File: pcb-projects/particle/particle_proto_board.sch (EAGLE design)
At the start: 53 parts, among them IC1 ATTINY20-MMH, IC2 DMC2400V, IC3 DMC2400V, SW1 SW1, SW2 SW2, SW3 SW3

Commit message: added several sparkfun and one samtec library, fixed #39, fixed #37, fixed #36, fixed #35, fixed #29
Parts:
- removed PI: 332-06, con-garry:332-06
- removed R3, R7, R8: J5MM, jumper:J5MM
- added J1: FTS-103-01-L-DV, samtec-FTS-103-01-L-DV:FTS-103-01-L-DV
- RESET: value RESET -> SWITCH-MOMENTARY-2SMD; device jumper-switches:SJ -> SparkFun-Electromechanical:SWITCH-MOMENTARY-2SMD
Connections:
- removed net N$16: R8.1, SW3.2
- removed net N$19: PI-4.S, R8.2
- removed net N$21: PI-1.S, R3.2
- net GND: now also J1.6, RESET.1, SGNL_LED.C; no longer PI-6.S, RESET.2, SWLED1.1
- net N$1: now also J1.1; no longer R3.1
- net N$11: now also SWLED1.2; no longer R5.1
- net N$15: now also J1.4, SW3.2; no longer PI-3.S, R7.2
- net N$20: now also J1.3; no longer R7.1
- net N$23: now also R5.1, SWLED1.1; no longer SGNL_LED.C, SWLED1.2
- net RESET: now also J1.5, RESET.2; no longer PI-5.S, RESET.1
- net VCC: now also J1.2; no longer PI-2.S
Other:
- moved on the sheet: C1, GND_A, GND_B, IC1B, IC2A, IC2B, IC3A, IC3B, PWR/TX_A, PWR/TX_B, PWR_LED, R1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

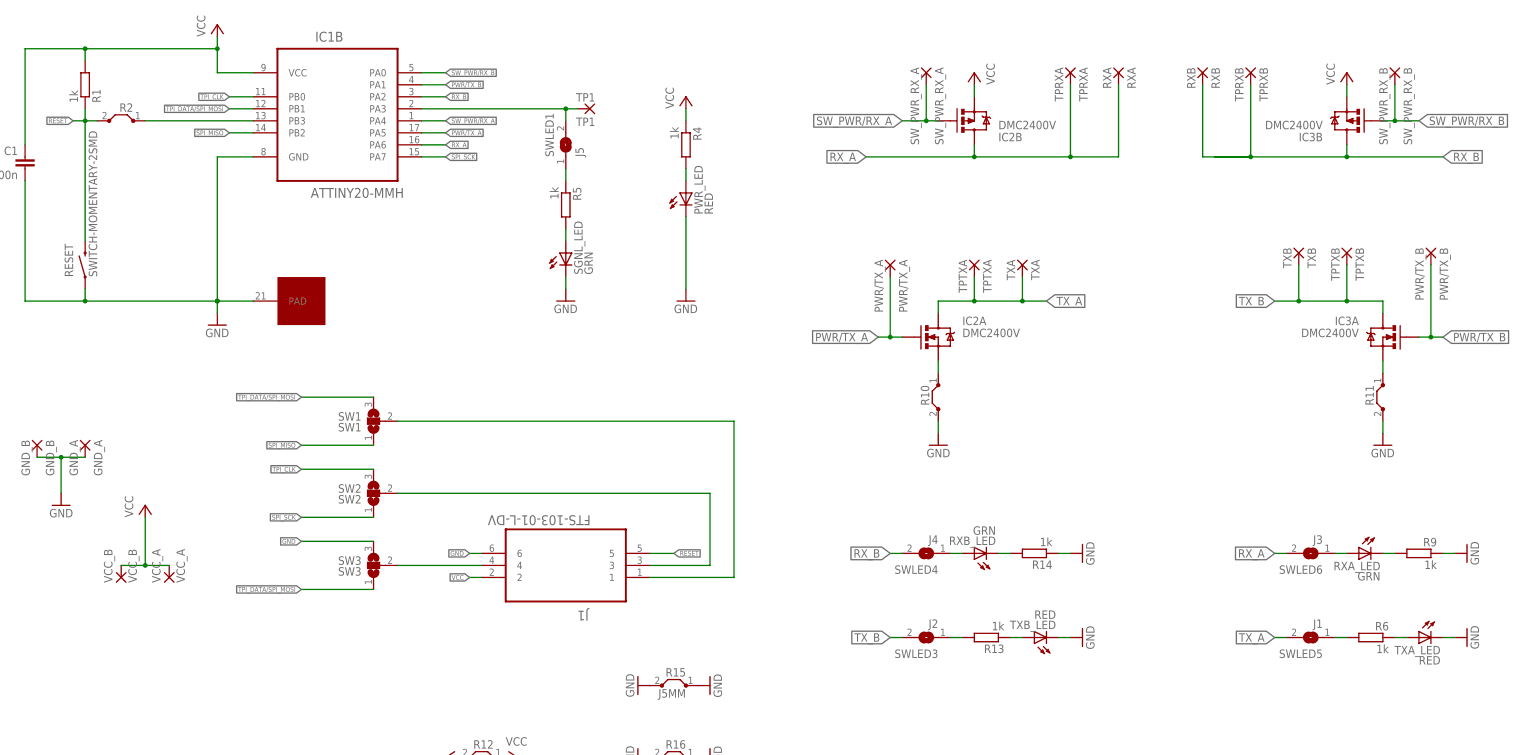
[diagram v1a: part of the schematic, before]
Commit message: fixed #41, fixed #40, fixed #39, fixed #37, fixed #35, fixed #29
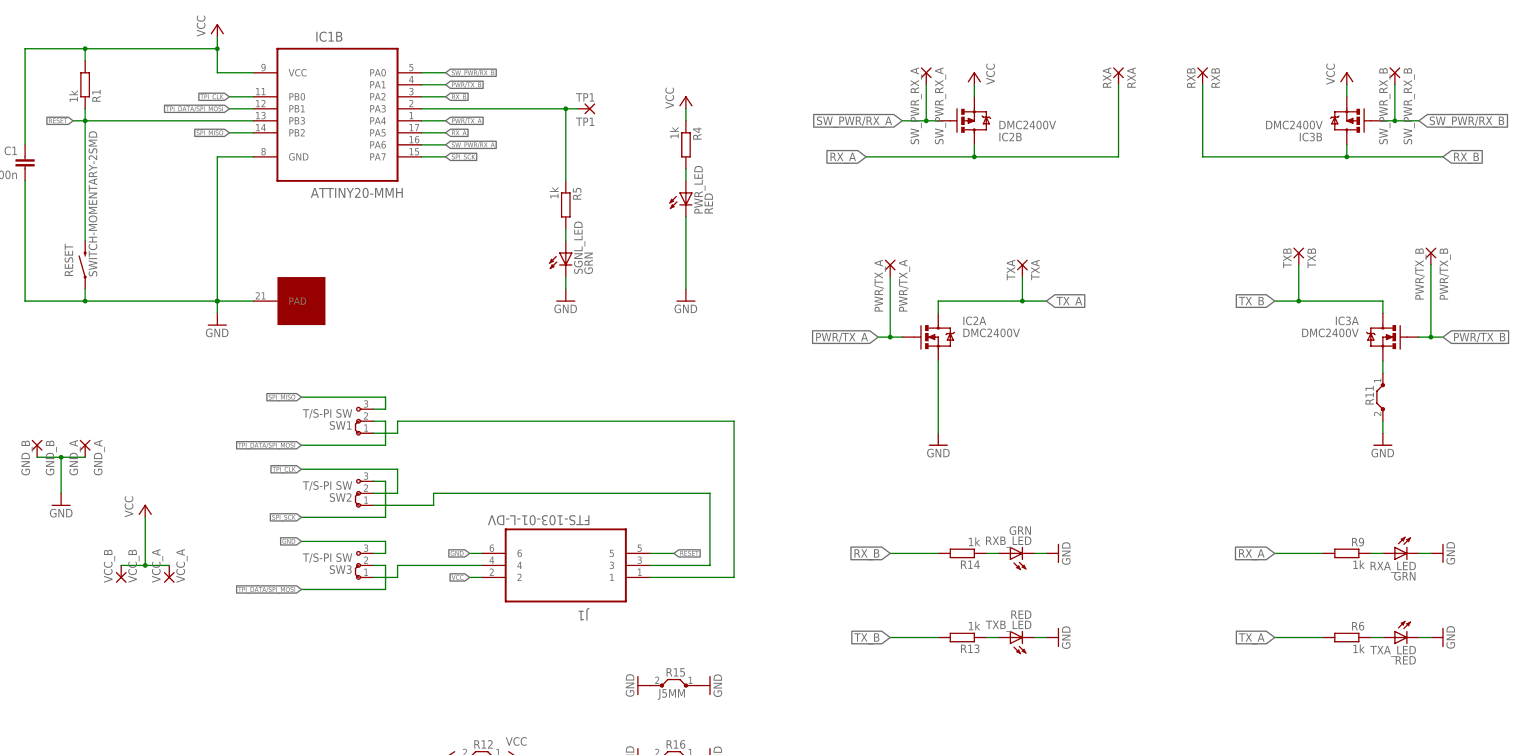
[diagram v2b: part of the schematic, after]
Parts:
- removed R10, R2: J5MM, jumper:J5MM
- removed SWLED1: J5, jumper-switches:SJ
- removed SWLED3: J2, jumper-switches:SJ
- removed SWLED4: J4, jumper-switches:SJ
- removed SWLED5: J1, jumper-switches:SJ
- removed SWLED6: J3, jumper-switches:SJ
- removed TPRXA: TPRXA, wirepad:1,6/0,9
- removed TPRXB: TPRXB, wirepad:1,6/0,9
- removed TPTXA: TPTXA, wirepad:1,6/0,9
- removed TPTXB: TPTXB, wirepad:1,6/0,9
- R1, R13, R14, R4, R5, R6, R9: device rcl:R-EU_R2010 -> rcl:R-EU_R1206
- SW1: value SW1 -> T/S-PI SW; device jumper-switches:SJ2W -> jumper-switches:J2X2MM
- SW2: value SW2 -> T/S-PI SW; device jumper-switches:SJ2W -> jumper-switches:J2X2MM
- SW3: value SW3 -> T/S-PI SW; device jumper-switches:SJ2W -> jumper-switches:J2X2MM
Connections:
- removed net N$11: IC1B.PA3, SWLED1.2, TP1.P
- removed net N$12: RXA_LED.A, SWLED6.1
- removed net N$14: R6.2, SWLED5.1
- removed net N$2: IC1B.PB3, R2.1
- removed net N$24: IC2A.S, R10.1
- removed net N$6: R13.2, SWLED3.1
- removed net N$7: RXB_LED.A, SWLED4.1
- net GND: now also IC2A.S, RXA_LED.C, RXB_LED.C; no longer R10.2, R14.1, R9.1
- net N$1: now also SW1.1; no longer SW1.2
- net N$15: now also SW3.1; no longer SW3.2
- net N$20: now also SW2.1; no longer SW2.2
- net N$23: now also IC1B.PA3, TP1.P; no longer SWLED1.1
- net N$4: now also R9.1, RXA_LED.A; no longer R9.2, RXA_LED.C
- net N$8: now also R14.1, RXB_LED.A; no longer R14.2, RXB_LED.C
- net PWR/TX_A: now also IC1B.PA4; no longer IC1B.PA5
- net RESET: now also IC1B.PB3; no longer R2.2
- net RX_A: now also IC1B.PA5, R9.2; no longer IC1B.PA6, SWLED6.2, TPRXA.P
- net RX_B: now also R14.2; no longer SWLED4.2, TPRXB.P
- net SPI_MISO: now also SW1.3; no longer SW1.1
- net SPI_SCK: now also SW2.3; no longer SW2.1
- net SW_PWR/RX_A: now also IC1B.PA6; no longer IC1B.PA4
- net TPI_CLK: now also SW2.2; no longer SW2.3
- net TPI_DATA/SPI_MOSI: now also SW1.2, SW3.2; no longer SW1.3, SW3.1
- net TX_A: now also R6.2; no longer SWLED5.2, TPTXA.P
- net TX_B: now also R13.2; no longer SWLED3.2, TPTXB.P
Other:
- moved on the sheet: R13, R14, R6, R9, RXA_LED, RXB_LED, SW1, SW2, SW3, TXA_LED, TXB_LED

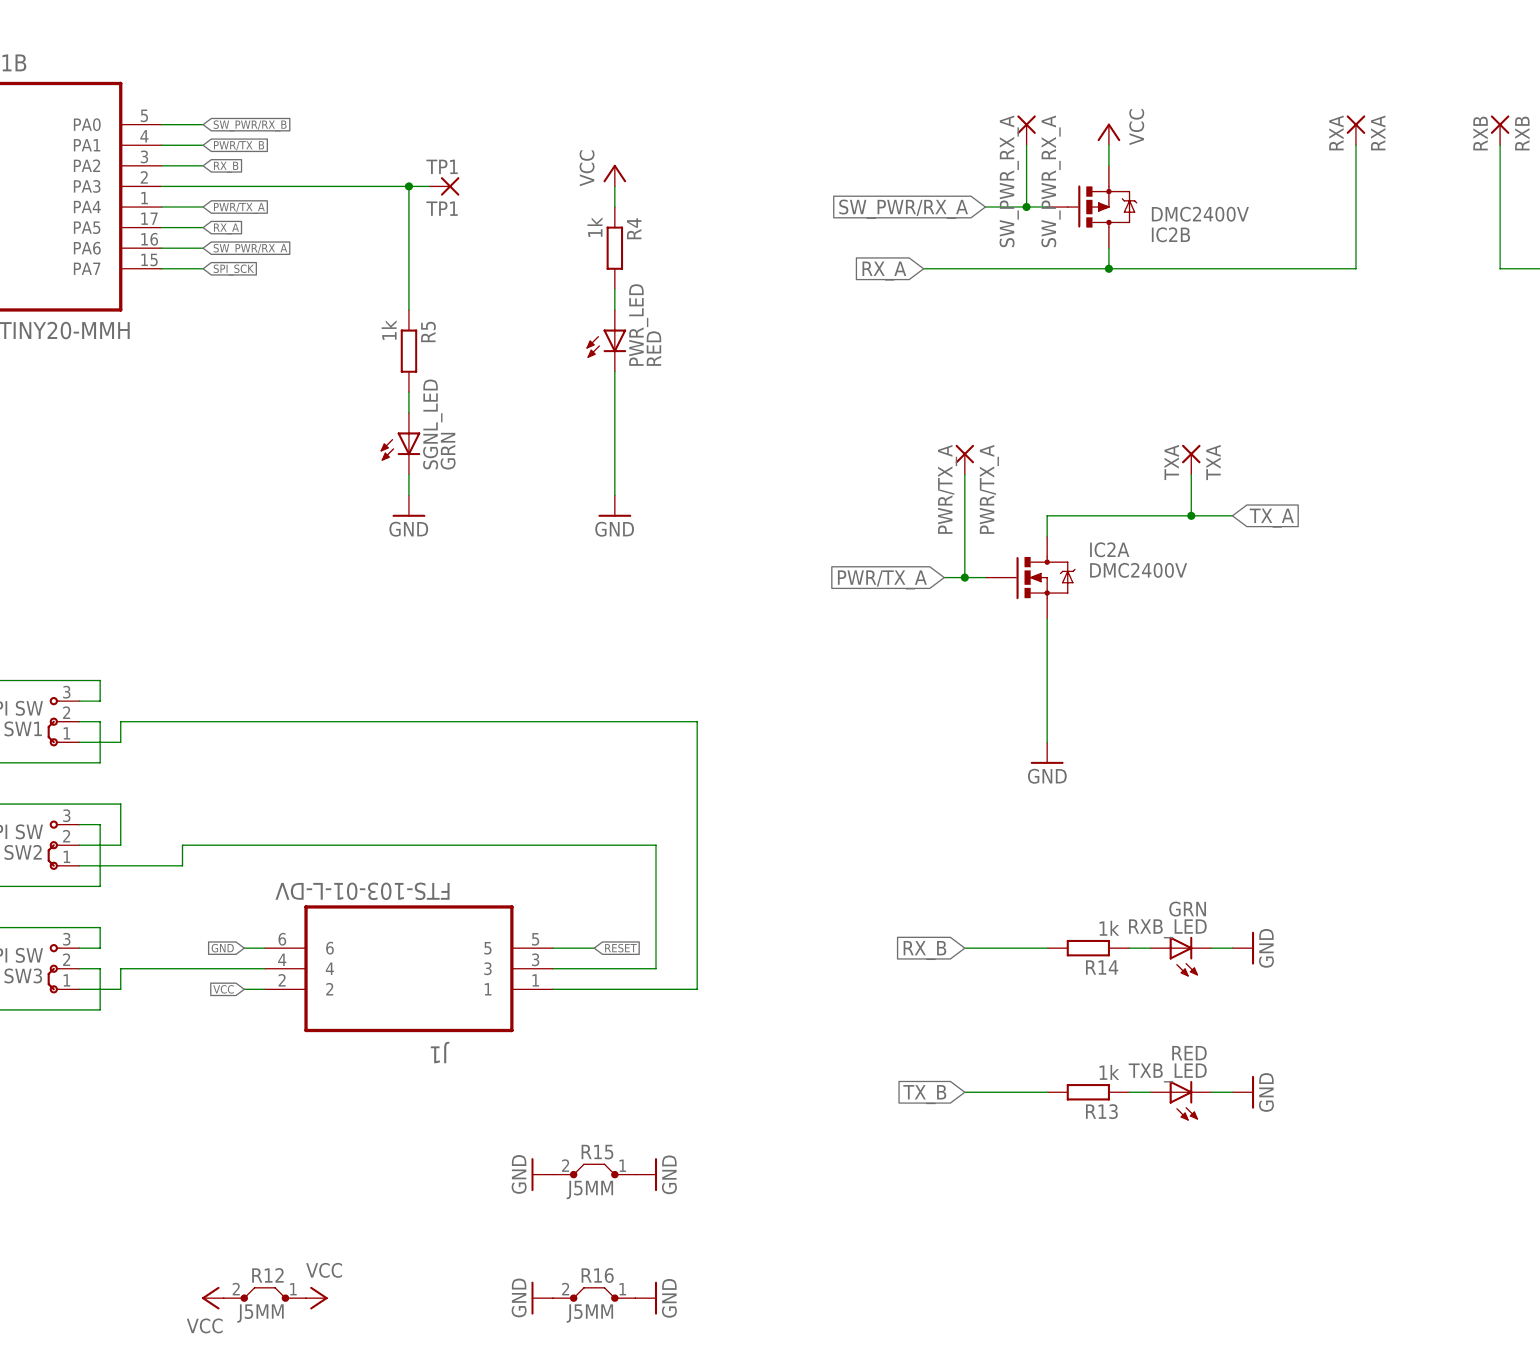
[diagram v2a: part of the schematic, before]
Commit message: routed board after several changes to schema
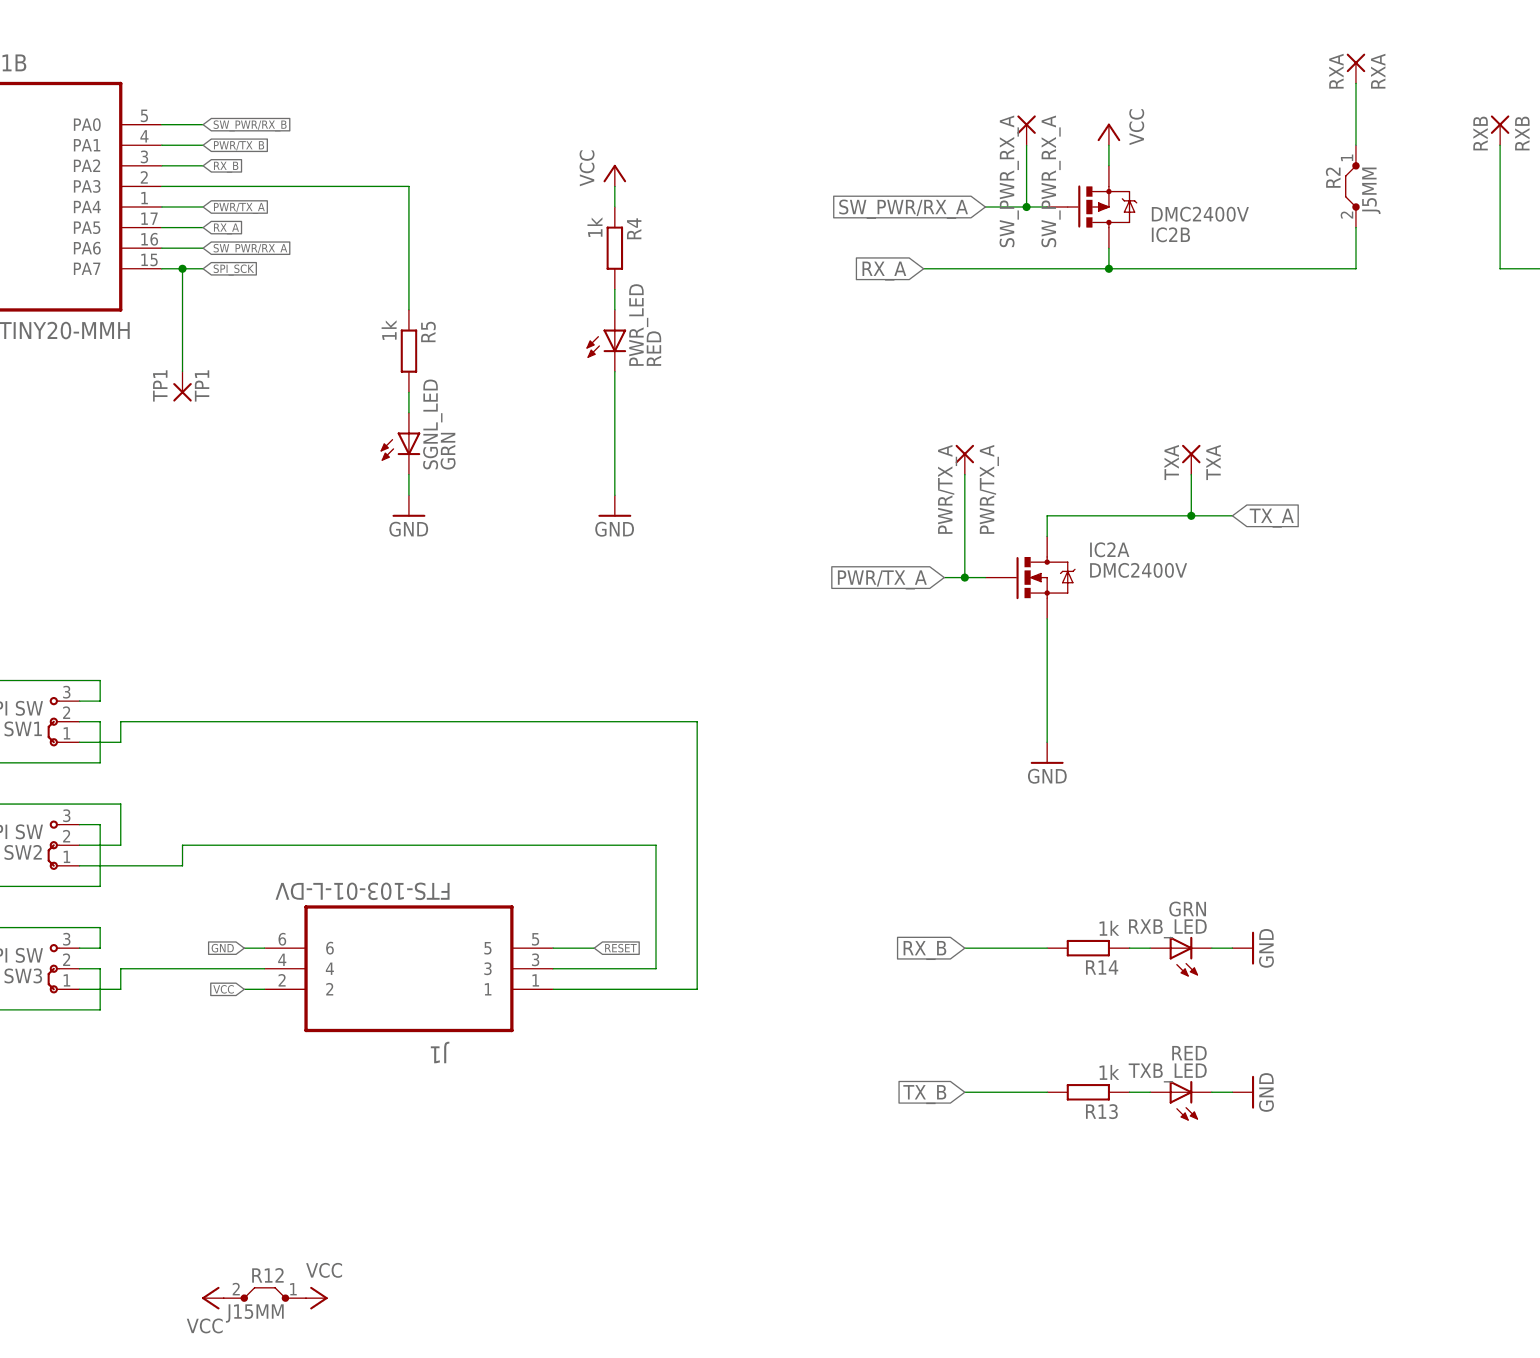
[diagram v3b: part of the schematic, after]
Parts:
- removed R15, R16: J5MM, jumper:J5MM
- added R2: J5MM, jumper:J5MM
- R12: value J5MM -> J15MM; device jumper:J5MM -> jumper:J15MM
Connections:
- new net N$2: R2.1, RXA.P
- net GND: no longer R15.1, R15.2, R16.1, R16.2
- net N$23: no longer TP1.P
- net RX_A: now also R2.2; no longer RXA.P
- net SPI_SCK: now also TP1.P
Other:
- moved on the sheet: RXA, TP1
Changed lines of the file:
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@@
 <part name="P+5" library="supply1" deviceset="VCC" device=""/>
 <part name="P+7" library="supply1" deviceset="VCC" device=""/>
-<part name="R12" library="jumper" deviceset="J" device="5MM" value="J5MM"/>
-<part name="GND9" library="supply1" deviceset="GND" device=""/>
-<part name="GND10" library="supply1" deviceset="GND" device=""/>
-<part name="GND11" library="supply1" deviceset="GND" device=""/>
-<part name="GND12" library="supply1" deviceset="GND" device=""/>
-<part name="R16" library="jumper" deviceset="J" device="5MM" value="J5MM"/>
-<part name="R15" library="jumper" deviceset="J" device="5MM" value="J5MM"/>
+<part name="R12" library="jumper" deviceset="J" device="15MM" value="J15MM"/>
 <part name="RESET" library="SparkFun-Electromechanical" deviceset="SWITCH-MOMENTARY-2" device="SMD"/>
 <part name="J1" library="samtec-FTS-103-01-L-DV" deviceset="FTS-103-01-L-DV" device=""/>
@@
 <part name="SW3" library="jumper-switches" deviceset="J2" device="X2MM" value="T/S-PI SW"/>
 <part name="SW2" library="jumper-switches" deviceset="J2" device="X2MM" value="T/S-PI SW"/>
+<part name="R2" library="jumper" deviceset="J" device="5MM" value="J5MM"/>
 </parts>
 <sheets>
@@
 <instance part="R1" gate="G$1" x="22.86" y="152.4" rot="MR90"/>
 <instance part="C1" gate="G$1" x="10.16" y="137.16" rot="MR0"/>
-<instance part="TP1" gate="1" x="129.54" y="147.32" rot="R180"/>
+<instance part="TP1" gate="1" x="96.52" y="121.92" rot="R90"/>
 <instance part="PWR/TX_A" gate="1" x="193.04" y="114.3" rot="R270"/>
 <instance part="SW_PWR_RX_A" gate="1" x="200.66" y="154.94" rot="R270"/>
@@
 <instance part="RXB" gate="1" x="259.08" y="154.94" rot="R270"/>
 <instance part="TXB" gate="1" x="279.4" y="116.84" rot="R270"/>
-<instance part="RXA" gate="1" x="241.3" y="154.94" rot="R270"/>
+<instance part="RXA" gate="1" x="241.3" y="162.56" rot="R270"/>
 <instance part="TXA" gate="1" x="220.98" y="114.3" rot="R270"/>
 <instance part="R4" gate="G$1" x="149.86" y="139.7" rot="R270"/>
@@
 <instance part="P+7" gate="VCC" x="114.3" y="10.16" rot="R270"/>
 <instance part="R12" gate="1" x="106.68" y="10.16" rot="MR0"/>
-<instance part="GND9" gate="1" x="139.7" y="25.4" rot="R270"/>
-<instance part="GND10" gate="1" x="154.94" y="25.4" rot="R90"/>
-<instance part="GND11" gate="1" x="139.7" y="10.16" rot="R270"/>
-<instance part="GND12" gate="1" x="154.94" y="10.16" rot="R90"/>
-<instance part="R16" gate="1" x="147.32" y="10.16" rot="MR0"/>
-<instance part="R15" gate="1" x="147.32" y="25.4" rot="MR0"/>
 <instance part="RESET" gate="G$1" x="22.86" y="114.3" rot="R90"/>
 <instance part="J1" gate="A" x="124.46" y="48.26" rot="R180"/>
@@
 <instance part="SW3" gate="G$1" x="81.28" y="50.8" rot="R180"/>
 <instance part="SW2" gate="G$1" x="81.28" y="66.04" rot="R180"/>
+<instance part="R2" gate="1" x="241.3" y="147.32" rot="MR270"/>
 </instances>
 <busses>
@@
 </segment>
 <segment>
-<pinref part="GND11" gate="1" pin="GND"/>
-<pinref part="R16" gate="1" pin="2"/>
-</segment>
-<segment>
-<pinref part="R16" gate="1" pin="1"/>
-<pinref part="GND12" gate="1" pin="GND"/>
-</segment>
-<segment>
-<pinref part="GND9" gate="1" pin="GND"/>
-<pinref part="R15" gate="1" pin="2"/>
-</segment>
-<segment>
-<pinref part="GND10" gate="1" pin="GND"/>
-<pinref part="R15" gate="1" pin="1"/>
-</segment>
-<segment>
 <pinref part="GND16" gate="1" pin="GND"/>
 <pinref part="SGNL_LED" gate="G$1" pin="C"/>
@@
 <segment>
 <pinref part="IC1" gate="B" pin="PA7"/>
-<wire x1="93.98" y1="137.16" x2="99.06" y2="137.16" width="0.1524" layer="91"/>
+<wire x1="93.98" y1="137.16" x2="96.52" y2="137.16" width="0.1524" layer="91"/>
 <label x="99.06" y="137.16" size="1.016" layer="95" xref="yes"/>
+<wire x1="96.52" y1="137.16" x2="99.06" y2="137.16" width="0.1524" layer="91"/>
+<wire x1="96.52" y1="124.46" x2="96.52" y2="137.16" width="0.1524" layer="91"/>
+<junction x="96.52" y="137.16"/>
+<pinref part="TP1" gate="1" pin="P"/>
 </segment>
 <segment>
@@
 <wire x1="210.82" y1="139.7" x2="210.82" y2="137.16" width="0.1524" layer="91"/>
 <junction x="210.82" y="137.16"/>
-<pinref part="RXA" gate="1" pin="P"/>
-<wire x1="241.3" y1="152.4" x2="241.3" y2="137.16" width="0.1524" layer="91"/>
+<pinref part="R2" gate="1" pin="2"/>
+<wire x1="241.3" y1="137.16" x2="241.3" y2="142.24" width="0.1524" layer="91"/>
 </segment>
 <segment>
@@
 <pinref part="R5" gate="G$1" pin="1"/>
 <wire x1="124.46" y1="132.08" x2="124.46" y2="147.32" width="0.1524" layer="91"/>
-<pinref part="TP1" gate="1" pin="P"/>
 <pinref part="IC1" gate="B" pin="PA3"/>
 <wire x1="93.98" y1="147.32" x2="124.46" y2="147.32" width="0.1524" layer="91"/>
-<wire x1="124.46" y1="147.32" x2="127" y2="147.32" width="0.1524" layer="91"/>
-<junction x="124.46" y="147.32"/>
 </segment>
 </net>
@@
 </segment>
 </net>
+<net name="N$2" class="0">
+<segment>
+<pinref part="RXA" gate="1" pin="P"/>
+<wire x1="241.3" y1="160.02" x2="241.3" y2="152.4" width="0.1524" layer="91"/>
+<pinref part="R2" gate="1" pin="1"/>
+</segment>
+</net>
